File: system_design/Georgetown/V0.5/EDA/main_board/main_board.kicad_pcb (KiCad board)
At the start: 2 copper layers, 40.6 x 78.5 mm, 28 parts, among them U1 top_rail_v2, U3 INA219AxD

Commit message: PCB modified
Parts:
- removed 5V: KA78M05_TO252, Package_TO_SOT_SMD:SOT-223-3_TabPin2
- removed ARDUINO NANO: Arduino_Nano_v2.x-MCU_Module, Module:Arduino_Nano
- removed CR-1025: Battery_Cell, custom:battery_holder_10mm
- removed DS3231: DS3231M, Package_SO:SOIC-16W_7.5x10.3mm_P1.27mm
- removed F1: Fuse, Resistor_SMD:R_0603_1608Metric_Pad1.05x0.95mm_HandSolder
- removed G***: LOGO, UofSC_logo:uofsc_logo_0_75in
- removed MICRO SD: small_microSD, custom:small_microSD_v2
- removed POWER: XP60PW, custom:XT60PW
- removed REF** (x4): MountingHole_3.2mm_M3, MountingHole:MountingHole_3.2mm_M3
- removed STAGE: HCSR04, custom:HCSR04
- removed switch1: grounded_switch, custom:grounded_switch
- added A1: Arduino_Nano_v2.x-MCU_Module, Module:Arduino_Nano, F.Cu at (143.3, 102.2)
- added BT1: Battery_Cell, ARTS-Lab:battery_holder_10mm, F.Cu at (167.1, 82.3)
- added J1: B3B-XH-A_LF__SN_, XH2.54:XH2.54, B.Cu at (170.7, 145.4)
- added P1: SD card socket, ST-TF-003A:SUNTECH_ST-TF-003A, B.Cu at (167.4, 79.5)
- added U2: DS3231M, Package_SO:SOIC-16W_7.5x10.3mm_P1.27mm, F.Cu at (144.9, 85.7)
- added U4: BME280_module, megasaturnv_custom_components:BME280_module, B.Cu at (148.0, 146.6)
- added U5: KA78M05_TO252, Package_TO_SOT_SMD:SOT-223-3_TabPin2, F.Cu at (169.9, 97.9)
- added Ultrasonic_sensor1: HCSR04, ARTS-Lab:HCSR04, F.Cu at (158.0, 146.3)
- U1: value top_rail_v2 -> HX-2S-JH10; footprint custom:top_rail_v2 -> megasaturnv_custom_components:HX-2S-JH10; moved to B.Cu
- moved R4 51.2 mm to (155.8, 77.7), turned to 180 degrees
- moved U1 45.3 mm to (169.6, 120.7), turned to -90 degrees
- moved R3 38.9 mm to (155.9, 89.7), turned to 180 degrees
- moved C3 23.5 mm to (175.8, 95.7), turned to -90 degrees
- moved nRF24L01+1 22.3 mm to (146.9, 85.4), turned to 180 degrees
- moved R2 18.7 mm to (165.9, 118.6)
- moved R5 17.0 mm to (155.9, 83.4), turned to 0 degrees
- moved C1 16.2 mm to (173.2, 109.8)
- moved R1 15.3 mm to (155.9, 94.8), turned to 180 degrees
- moved D2 13.8 mm to (146.5, 95.1)
- moved C4 12.6 mm to (166.0, 109.7), turned to -90 degrees
- moved U3 12.2 mm to (171.3, 129.0)
- moved D1 10.2 mm to (169.5, 118.7), turned to 90 degrees
- moved C2 9.41 mm to (165.8, 127.5)
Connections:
- C1 pad 1: Net-(A1-Pad17) -> Net-(A1-3V3)
- C2 pad 1: Net-(C2-Pad1) -> Net-(D1-K)
- C3 pad 2: Net-(A1-Pad30) -> Net-(A1-VIN)
- D1 pad 1: Net-(D1-Pad1) -> Net-(D1-K)
- D1 pad 2: Net-(D1-Pad2) -> Net-(D1-A)
- R2 pad 1: Net-(C2-Pad1) -> Net-(D1-K)
- R3 pad 1: Net-(A1-Pad17) -> Net-(A1-3V3)
- R3 pad 2: Net-(A1-Pad23) -> Net-(A1-A4)
- R4 pad 1: Net-(A1-Pad17) -> Net-(A1-3V3)
- R4 pad 2: Net-(A1-Pad24) -> Net-(A1-A5)
- R5 pad 2: Net-(A1-Pad17) -> Net-(A1-3V3)
- U1 pad 2: Net-(A1-Pad24) -> Net-(D1-A)
- U1 pad 3: Net-(A1-Pad23) -> unconnected-(U1-B--Pad3)
- U1 pad 4: Net-(A1-Pad30) -> unconnected-(U1-BM-Pad4)
- U1 pad 5: Net-(A1-Pad17) -> unconnected-(U1-B+-Pad5)
- U3 pad 1: Net-(U3-Pad1) -> unconnected-(U3-A1-Pad1)
- U3 pad 2: Net-(U3-Pad2) -> unconnected-(U3-A0-Pad2)
- U3 pad 3: Net-(A1-Pad23) -> Net-(A1-A4)
- U3 pad 4: Net-(A1-Pad24) -> Net-(A1-A5)
- U3 pad 5: Net-(A1-Pad17) -> Net-(A1-3V3)
- U3 pad 8: Net-(C2-Pad1) -> Net-(D1-K)
- nRF24L01+1 pad 1: Net-(A1-Pad17) -> Net-(A1-3V3)
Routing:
- net Net-(A1-Pad17): track 109.2 -> 0.00 mm, vias 3 -> 0
- net Net-(A1-Pad24): track 97.5 -> 0.00 mm, vias 4 -> 0
- net Net-(A1-Pad30): track 94.6 -> 0.00 mm, vias 2 -> 0
- net Net-(A1-Pad23): track 87.2 -> 0.00 mm, vias 3 -> 0
- net Net-(A1-D13): track 56.3 -> 0.00 mm, vias 3 -> 0
- net Net-(A1-Pad7): track 54.6 -> 0.00 mm
- net Net-(A1-Pad8): track 52.6 -> 0.00 mm
- net Net-(A1-D11): track 48.0 -> 0.00 mm
- net Net-(A1-D2): track 46.0 -> 0.00 mm, vias 1 -> 0
- net Net-(A1-Pad13): track 45.1 -> 0.00 mm
- net Net-(A1-D12): track 43.4 -> 0.00 mm, vias 1 -> 0
- net Net-(A1-Pad11): track 36.6 -> 0.00 mm
- net Net-(A1-Pad12): track 36.6 -> 0.00 mm
- net Net-(A1-A3): track 35.4 -> 0.00 mm, vias 3 -> 0
- net Net-(U3-IN-): track 30.4 -> 0.00 mm
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- removed copper zone on B.Cu, net GND
- removed copper zone on F.Cu, net GND
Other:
- board text added: "V0.5"
- board text removed: "MB V0.4"
- board text removed: "OFF"

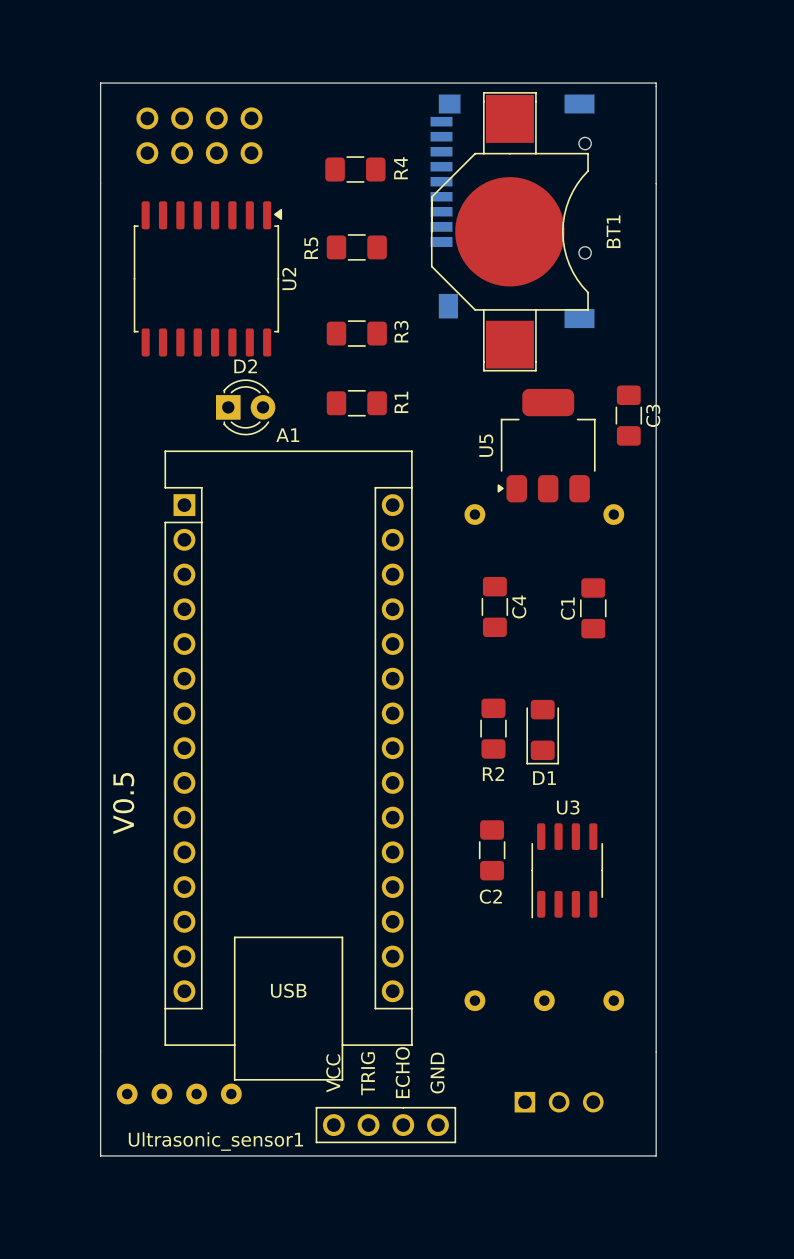
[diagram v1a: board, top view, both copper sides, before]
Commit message: CAD updated
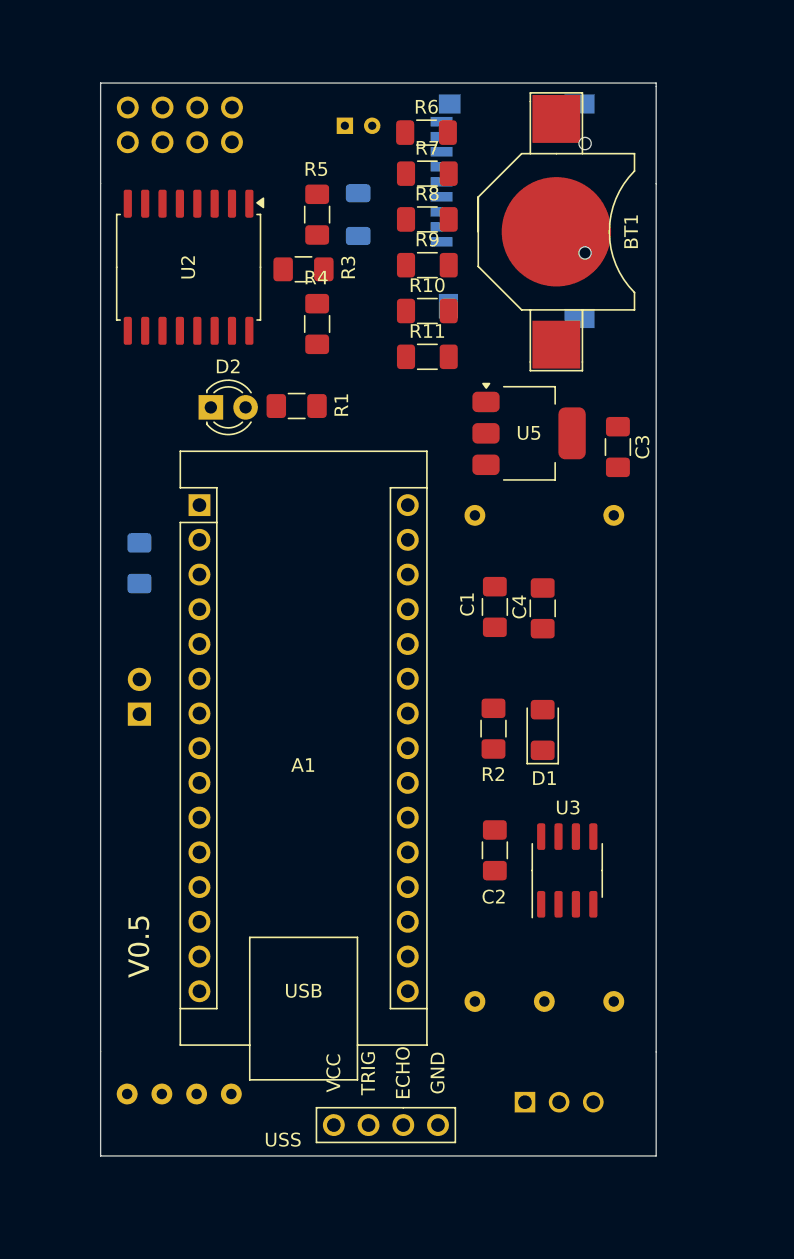
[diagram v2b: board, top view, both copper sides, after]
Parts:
- added C5: 10uF, Capacitor_THT:CP_Radial_D4.0mm_P2.00mm, B.Cu at (155.0, 74.5)
- added C6: 0.1uF, Capacitor_SMD:C_1206_3216Metric_Pad1.33x1.80mm_HandSolder, B.Cu at (156.0, 81.0)
- added D1: D_Schottky, Diode_SMD:D_1206_3216Metric_Pad1.42x1.75mm_HandSolder, B.Cu at (140.0, 106.5)
- added J2: Conn_01x02_Pin, Connector_PinHeader_2.54mm:PinHeader_1x02_P2.54mm_Vertical, B.Cu at (140.0, 117.5)
- added R10: 2K, Capacitor_SMD:C_1206_3216Metric_Pad1.33x1.80mm_HandSolder, F.Cu at (161.1, 88.0)
- added R11: 1K, Capacitor_SMD:C_1206_3216Metric_Pad1.33x1.80mm_HandSolder, F.Cu at (161.1, 91.4)
- added R6: 2K, Capacitor_SMD:C_1206_3216Metric_Pad1.33x1.80mm_HandSolder, F.Cu at (161.0, 75.0)
- added R7: 1K, Capacitor_SMD:C_1206_3216Metric_Pad1.33x1.80mm_HandSolder, F.Cu at (161.1, 78.0)
- added R8: 2K, Capacitor_SMD:C_1206_3216Metric_Pad1.33x1.80mm_HandSolder, F.Cu at (161.1, 81.3)
- added R9: 1K, Capacitor_SMD:C_1206_3216Metric_Pad1.33x1.80mm_HandSolder, F.Cu at (161.1, 84.7)
- moved R4 11.6 mm to (153.0, 89.0), turned to -90 degrees
- moved R3 6.11 mm to (152.0, 85.0)
- moved R1 4.40 mm to (151.5, 95.0)
- moved R5 3.76 mm to (153.0, 81.0), turned to -90 degrees
- moved C1 3.70 mm to (169.5, 109.8)
- moved BT1 3.40 mm to (170.5, 82.3)
- moved C3 2.44 mm to (175.0, 98.0)
- moved U5 1.66 mm to (168.5, 97.0), turned to 0 degrees
- moved nRF24L01+1 1.64 mm to (145.5, 84.6)
- moved U2 1.56 mm to (143.6, 84.8)
- moved D2 1.28 mm to (145.2, 95.1)
- moved A1 1.10 mm to (144.4, 102.2)
- moved C2 0.20 mm to (166.0, 127.5)
- moved U1 0.06 mm to (169.6, 120.8)
- renumbered Ultrasonic_sensor1 to USS
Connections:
- A1 pad 13: unconnected-(A1-D10-Pad13) -> Net-(A1-D10)
- A1 pad 27: unconnected-(A1-+5V-Pad27) -> Net-(A1-+5V)
- A1 pad 30: Net-(A1-VIN) -> unconnected-(A1-VIN-Pad30)
- C3 pad 2: Net-(A1-VIN) -> Net-(A1-+5V)
- J1 pad 1: unconnected-(J1-Pad1) -> Net-(U1-B+)
- J1 pad 2: unconnected-(J1-Pad2) -> Net-(U1-BM)
- J1 pad 3: unconnected-(J1-Pad3) -> Net-(U1-B-)
- P1 pad 2: unconnected-(P1-DAT3/CS-Pad2) -> Net-(P1-DAT3/CS)
- P1 pad 3: unconnected-(P1-CMD/MOSI-Pad3) -> Net-(P1-CMD/MOSI)
- P1 pad 5: unconnected-(P1-CLK/SCK-Pad5) -> Net-(P1-CLK/SCK)
- U1 pad 2: Net-(D1-A) -> Net-(D1-K)
- U1 pad 3: unconnected-(U1-B--Pad3) -> Net-(U1-B-)
- U1 pad 4: unconnected-(U1-BM-Pad4) -> Net-(U1-BM)
- U1 pad 5: unconnected-(U1-B+-Pad5) -> Net-(U1-B+)
- U4 pad 1: unconnected-(U4-VIN-Pad1) -> Net-(A1-3V3)
- U4 pad 2: unconnected-(U4-GND-Pad2) -> GND
- U4 pad 3: unconnected-(U4-SCL-Pad3) -> Net-(A1-A5)
- U4 pad 4: unconnected-(U4-SDA-Pad4) -> Net-(A1-A4)
- U5 pad 3: Net-(A1-VIN) -> Net-(A1-+5V)
- USS pad 4: Net-(A1-VIN) -> Net-(A1-+5V)
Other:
- board text added: "+"
- board text added: "SOL IN"

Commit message: PCB design changed
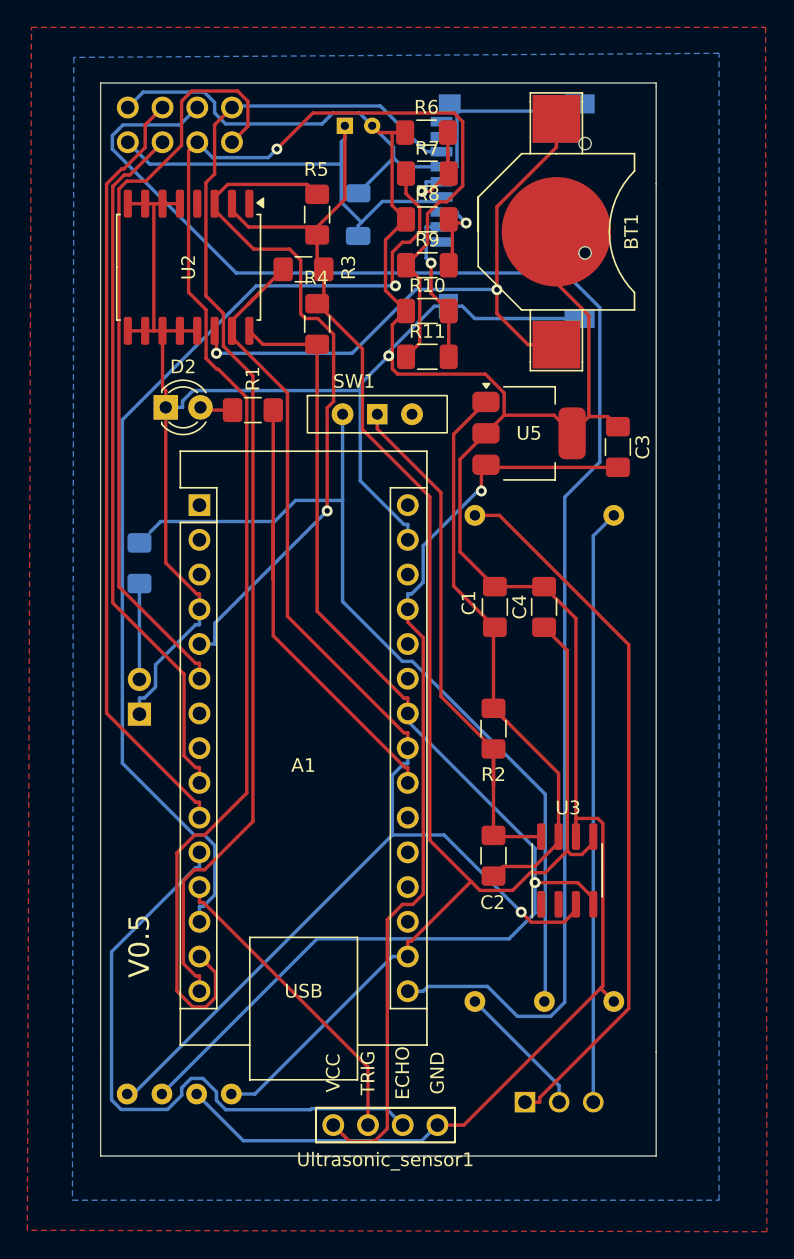
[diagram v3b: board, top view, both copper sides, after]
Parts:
- removed the D1 at (169.5, 118.7)
- removed USS: HCSR04, ARTS-Lab:HCSR04
- added SW1: SW_Wuerth_450301014042, Button_Switch_THT:SW_Slide-03_Wuerth-WS-SLTV_10x2.5x6.4_P2.54mm, F.Cu at (157.4, 95.6)
- added Ultrasonic_sensor1: HCSR04, ARTS-Lab:HCSR04, F.Cu at (158.0, 146.3)
- moved D2 3.30 mm to (141.9, 95.1)
- moved R1 3.21 mm to (148.3, 95.3)
- moved C2 0.41 mm to (165.9, 127.9)
- moved C1 0.14 mm to (169.6, 109.7)
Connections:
- C2 pad 1: Net-(D1-K) -> Net-(SW1-B)
- R2 pad 1: Net-(D1-K) -> Net-(SW1-B)
- U3 pad 8: Net-(D1-K) -> Net-(SW1-B)
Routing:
- net GND: track 0.00 -> 288.6 mm, vias 0 -> 1
- net Net-(A1-3V3): track 0.00 -> 153.7 mm
- net Net-(A1-D11): track 0.00 -> 115.4 mm, vias 0 -> 1
- net Net-(A1-D13): track 0.00 -> 113.4 mm
- net Net-(A1-A4): track 0.00 -> 94.4 mm, vias 0 -> 1
- net Net-(A1-A5): track 0.00 -> 91.7 mm, vias 0 -> 1
- net Net-(A1-D12): track 0.00 -> 86.8 mm
- net Net-(A1-D10): track 0.00 -> 74.5 mm, vias 0 -> 1
- net Net-(A1-+5V): track 0.00 -> 67.7 mm, vias 0 -> 1
- net Net-(D1-K): track 0.00 -> 64.6 mm
- net Net-(A1-D7): track 0.00 -> 56.7 mm
- net Net-(A1-D3): track 0.00 -> 56.5 mm
- net Net-(U1-B+): track 0.00 -> 52.4 mm
- net Net-(A1-D6): track 0.00 -> 51.4 mm
- net Net-(A1-D2): track 0.00 -> 51.3 mm, vias 0 -> 1
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- added copper zone on B.Cu, net GND
- added copper zone on F.Cu, net GND
